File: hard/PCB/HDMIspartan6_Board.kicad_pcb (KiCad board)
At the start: 4 copper layers, 60 x 85.1 mm, 167 parts, among them IC1 W9812G6KH, J1 HDMI_A, P1 CONN_01X03, P2 CONN_01X02, P3 CONN_02X02, P4 CONN_02X02, P5 CONN_01X03, P6 CONN_01X03, P7 B6B-PH-K-S(LF)(SN), SW1 B3SL-1002P, U1 PAM8302AASCR, U2 TPS63070, X1 ASV-32.000MHZ-E-T

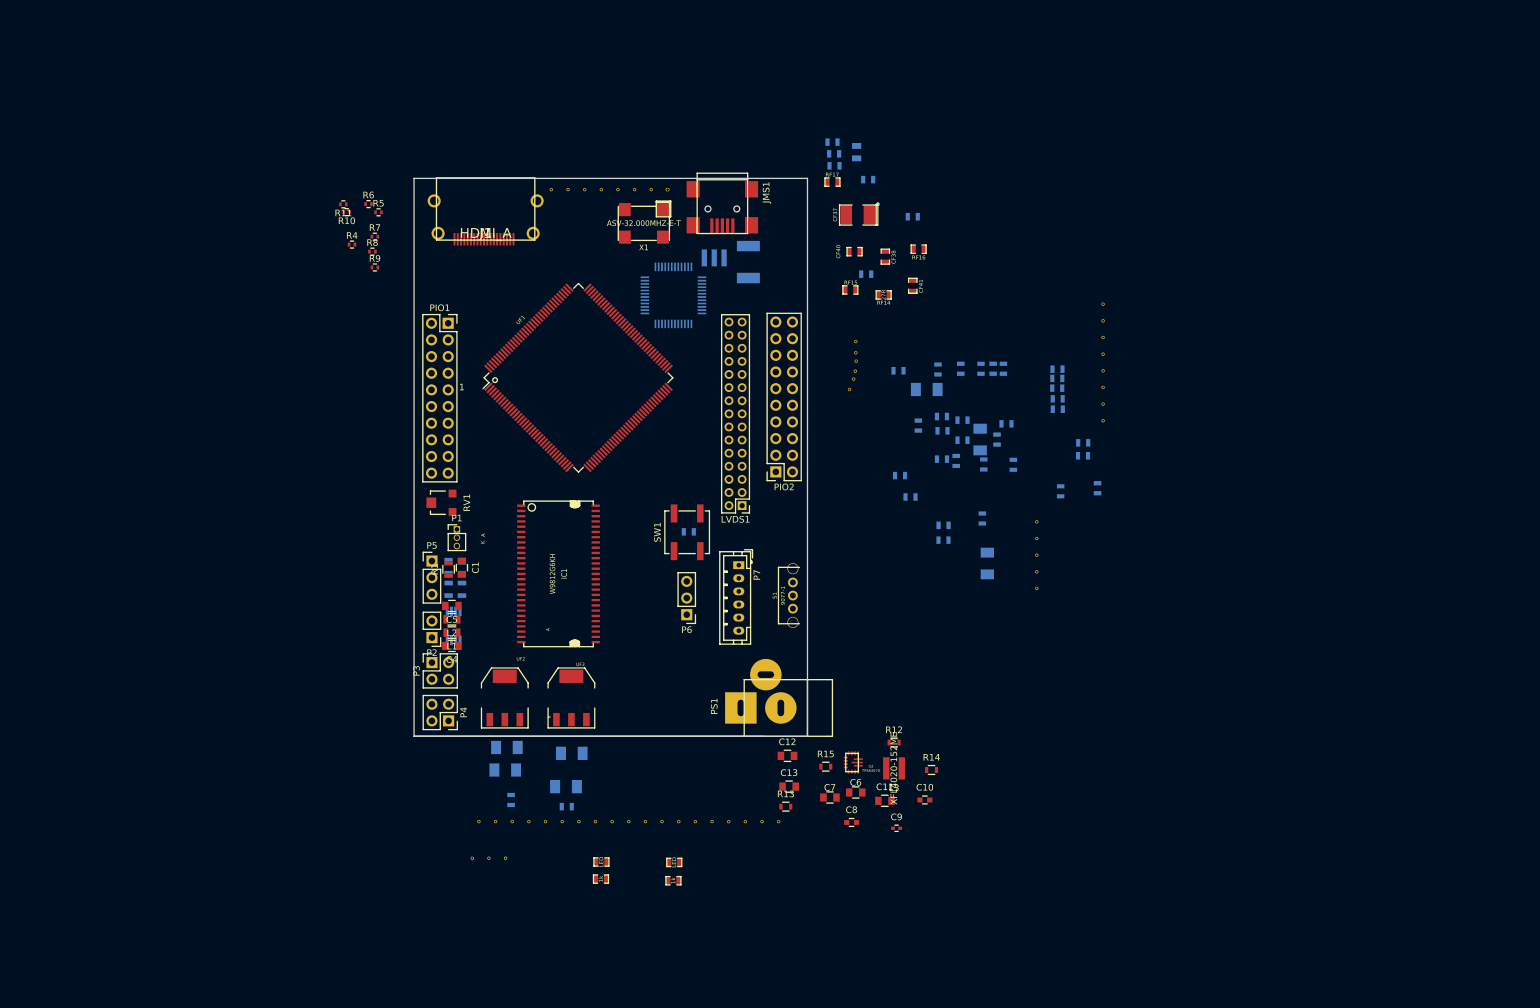
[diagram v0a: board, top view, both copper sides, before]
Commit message: Update supply power
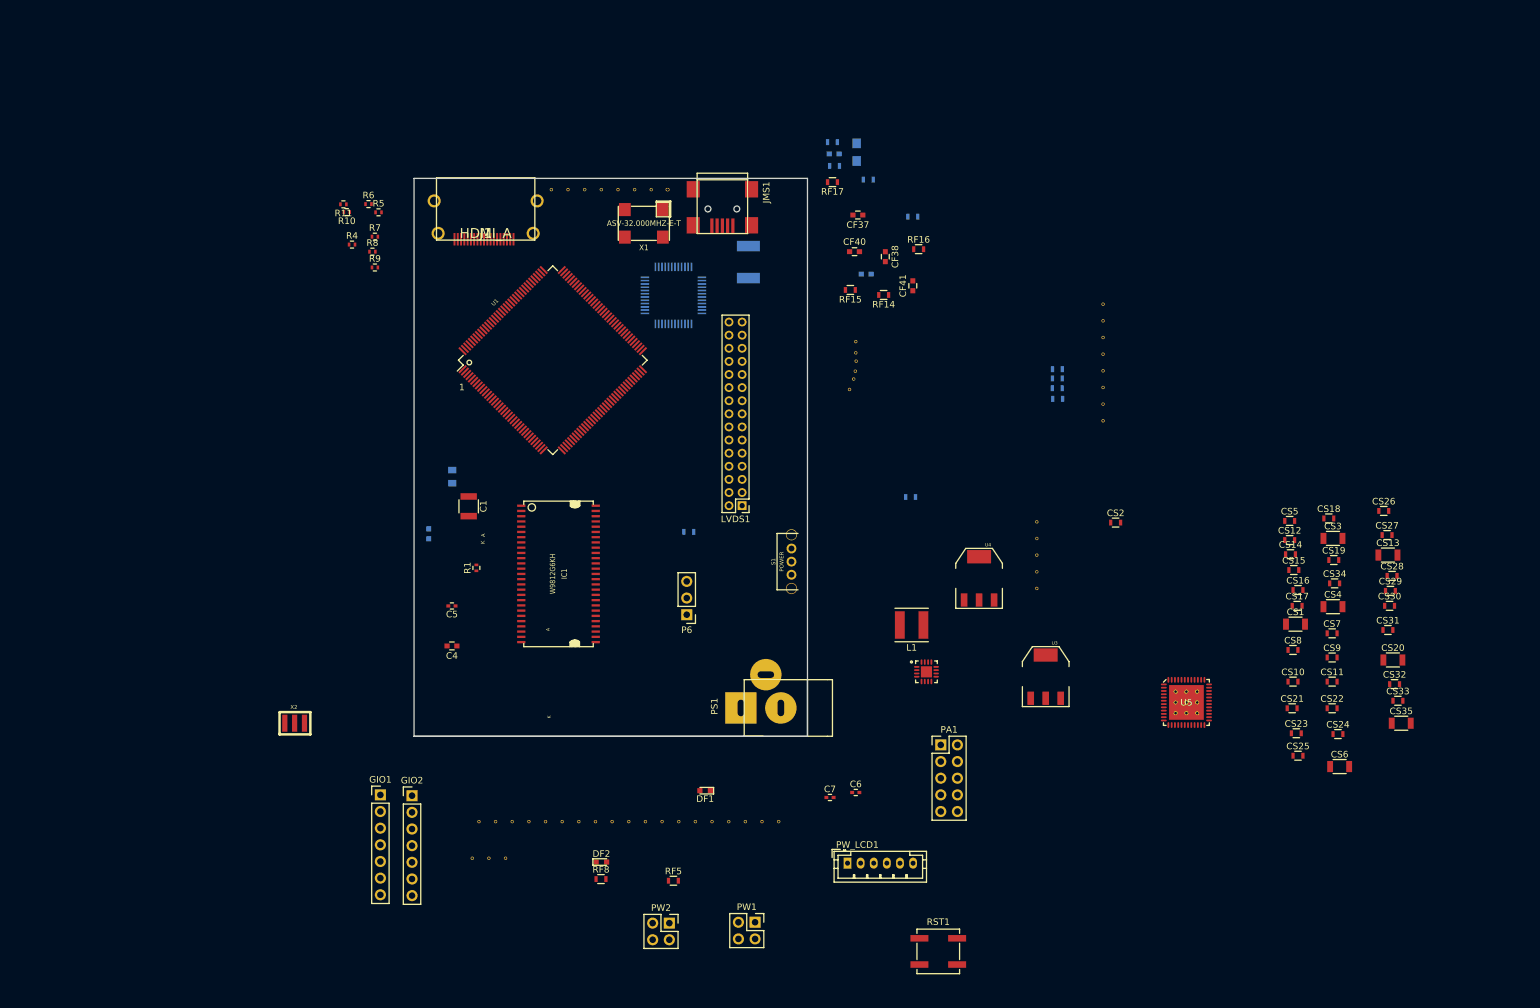
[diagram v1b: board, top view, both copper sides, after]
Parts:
- removed C10, C8: 10u, Capacitors_SMD:C_0603
- removed C11, C12, C13: 22u, Capacitors_SMD:C_0805
- removed C9: 100n, Capacitors_SMD:C_0402
- removed CF1, CF10, CF12, CF14, CF15, CF16, CF17, CF18, CF19, CF2, CF20, CF21, CF22, CF23, CF24, CF25, CF3, CF4, CF5, CF6, CF7, CF8, CF9: 0.1uF, opendous:SM0603
- removed CF11, CF26, CF27: 1uF, opendous:SM0603
- removed CF13, CF28, CF29: 4.7uF, opendous:SM1206_Opendous
- removed CF30, CF32, CF33, CF35: 33uF, opendous:SM1206_Opendous
- removed CF31, CF34: 100n, opendous:SM0603
- removed L2: Ferrite_Bead, Resistors_SMD:R_0805
- removed L3: XFL4020-152ME, resonator:XFL4020
- removed P1: CONN_01X03, Socket_Strips:Socket_Strip_Straight_1x03_Pitch1.27mm
- removed P2: CONN_01X02, Socket_Strips:Socket_Strip_Straight_1x02_Pitch2.54mm
- removed P3, P4: CONN_02X02, Socket_Strips:Socket_Strip_Straight_2x02_Pitch2.54mm
- removed P5: CONN_01X03, Socket_Strips:Socket_Strip_Straight_1x03_Pitch2.54mm
- removed P7: B6B-PH-K-S(LF)(SN), Connectors_JST:JST_PH_B6B-PH-K_06x2.00mm_Straight
- removed PIO1, PIO2: CONN_02X10, Socket_Strips:Socket_Strip_Straight_2x10_Pitch2.54mm
- removed R12: 10k, Resistors_SMD:R_0603
- removed R13: 680k, Resistors_SMD:R_0603
- removed R14: 130k, Resistors_SMD:R_0603
- removed R15: 100k, Resistors_SMD:R_0603
- removed R2, R3: 100, Resistors_SMD:R_0805
- removed RV1: 10K POT_TRIM, Potentiometers:Potentiometer_Trimmer-EVM3E
- removed SW1: B3SL-1002P, Buttons_Switches_SMD:SW_SPST_B3SL-1002P
- removed UF1: XC6SLX9-2TQG144C, Housings_QFP:LQFP-144_20x20mm_Pitch0.5mm
- removed UF2: ZLDO1117G33TA, SMD_Packages:SOT-223
- removed UF3: ZLDO1117G12TA, SMD_Packages:SOT-223
- removed XF2: 6MHz, resonator:CSTCR6M00G53Z
- added CS1: 33uF, Resistors_SMD:R_1206, F.Cu at (192.7, 100.0)
- added CS10: 0.1uF, Resistors_SMD:R_0603, F.Cu at (192.3, 108.7)
- added CS11: 0.1uF, Resistors_SMD:R_0603, F.Cu at (198.2, 108.7)
- added CS12: 1uF, Resistors_SMD:R_0603, F.Cu at (191.8, 87.1)
- added CS13: 4.7uF, Resistors_SMD:R_1206, F.Cu at (206.8, 89.4)
- added CS14: 1uF, Resistors_SMD:R_0603, F.Cu at (191.9, 89.3)
- added CS15: 1uF, Resistors_SMD:R_0603, F.Cu at (192.4, 91.7)
- added CS16: 1uF, Resistors_SMD:R_0603, F.Cu at (193.0, 94.7)
- added CS17: 1uF, Resistors_SMD:R_0603, F.Cu at (192.9, 97.2)
- added CS18: 1uF, Resistors_SMD:R_0603, F.Cu at (197.7, 83.8)
- added CS19: 1uF, Resistors_SMD:R_0603, F.Cu at (198.5, 90.2)
- added CS2: 100n, Resistors_SMD:R_0603, F.Cu at (165.2, 84.5)
- added CS20: 4.7uF, Resistors_SMD:R_1206, F.Cu at (207.5, 105.4)
- added CS21: 0.1uF, Resistors_SMD:R_0603, F.Cu at (192.2, 112.8)
- added CS22: 0.1uF, Resistors_SMD:R_0603, F.Cu at (198.2, 112.8)
- added CS23: 0.1uF, Resistors_SMD:R_0603, F.Cu at (192.8, 116.6)
- added CS24: 0.1uF, Resistors_SMD:R_0603, F.Cu at (199.1, 116.7)
- added CS25: 0.1uF, Resistors_SMD:R_0603, F.Cu at (193.0, 120.0)
- added CS26: 0.1uF, Resistors_SMD:R_0603, F.Cu at (206.1, 82.7)
- added CS27: 0.1uF, Resistors_SMD:R_0603, F.Cu at (206.6, 86.4)
- added CS28: 0.1uF, Resistors_SMD:R_0603, F.Cu at (207.4, 92.6)
- added CS29: 0.1uF, Resistors_SMD:R_0603, F.Cu at (207.1, 94.9)
- added CS3: 33uF, Resistors_SMD:R_1206, F.Cu at (198.4, 86.9)
- added CS30: 0.1uF, Resistors_SMD:R_0603, F.Cu at (207.0, 97.2)
- added CS31: 0.1uF, Resistors_SMD:R_0603, F.Cu at (206.8, 100.8)
- added CS32: 0.1uF, Resistors_SMD:R_0603, F.Cu at (207.8, 109.1)
- added CS33: 0.1uF, Resistors_SMD:R_0603, F.Cu at (208.3, 111.6)
- added CS34: 1uF, Resistors_SMD:R_0603, F.Cu at (198.6, 93.7)
- added CS35: 4.7uF, Resistors_SMD:R_1206, F.Cu at (208.8, 115.1)
- added CS4: 33uF, Resistors_SMD:R_1206, F.Cu at (198.4, 97.3)
- added CS5: 100n, Resistors_SMD:R_0603, F.Cu at (191.8, 84.2)
- added CS6: 33uF, Resistors_SMD:R_1206, F.Cu at (199.4, 121.7)
- added CS7: 0.1uF, Resistors_SMD:R_0603, F.Cu at (198.2, 101.3)
- added CS8: 0.1uF, Resistors_SMD:R_0603, F.Cu at (192.3, 103.9)
- added CS9: 0.1uF, Resistors_SMD:R_0603, F.Cu at (198.2, 105.0)
- added GIO1: CONN_01X07, Pin_Headers:Pin_Header_Straight_1x07_Pitch2.54mm, F.Cu at (53.1, 126.0)
- added GIO2: CONN_01X07, Pin_Headers:Pin_Header_Straight_1x07_Pitch2.54mm, F.Cu at (57.9, 126.1)
- added PA1: CONN_02X05, Pin_Headers:Pin_Header_Straight_2x05_Pitch2.54mm, F.Cu at (138.6, 118.4)
- added PW1: CONN_02X02, Socket_Strips:Socket_Strip_Straight_2x02_Pitch2.54mm, F.Cu at (110.2, 145.4)
- added PW2: CONN_02X02, Socket_Strips:Socket_Strip_Straight_2x02_Pitch2.54mm, F.Cu at (97.2, 145.5)
- added PW_LCD1: B6B-PH-K-S(LF)(SN), Connectors_JST:JST_PH_B6B-PH-K_06x2.00mm_Straight, F.Cu at (124.3, 136.4)
- added RST1: B3SL-1002P, Buttons_Switches_SMD:SW_SPST_B3SL-1002P, F.Cu at (138.2, 149.9)
- added U3: ZLDO1117G33TA, Project:SOT-223, F.Cu at (154.6, 108.0)
- added U4: ZLDO1117G12TA, Project:SOT-223, F.Cu at (144.4, 93.0)
- added U5: MAX5864, Project:GSG-QFN48-7, F.Cu at (176.0, 111.9)
- added X2: CSTCR6M00G53Z-R0, Project:CSTCR6M00G53Z, F.Cu at (40.0, 115.1)
- C1: footprint Capacitors_SMD:C_0805 -> Capacitors_SMD:C_1210
- C2: value 1uF -> 100nF; footprint Capacitors_SMD:C_0805 -> Capacitors_SMD:C_0603
- C3: value 1uF -> 22uF
- C4: value 220pF -> 3.3nF; footprint Capacitors_SMD:C_0805 -> Capacitors_SMD:C_0603
- C5: value 220pF -> 330nF; footprint Capacitors_SMD:C_0805 -> Capacitors_SMD:C_0402
- C6, C7: value 10u -> 330nF; footprint Capacitors_SMD:C_0805 -> Capacitors_SMD:C_0402
- CF36, CF38, CF39, CF40, CF41: footprint opendous:SM0603_Opendous -> Capacitors_SMD:C_0603
- CF37: footprint opendous:SM1210_Opendous -> Capacitors_SMD:C_0603
- DF1, DF2: footprint opendous:SM0603 -> LEDs:LED_0603
- FT1: footprint Housings_QFP:LQFP-48_7x7mm_Pitch0.5mm -> Project:LQFP-48_7x7mm_Pitch0.5mm
- IC1: footprint opendous:TSOPII54_SDRAM_MT48 -> Project:TSOPII54_SDRAM_MT48
- J1: footprint HDMI:FCI_10029449-11[13]RLF -> Project:HDMI_FCI_10029449-11[13]RLF
- JMS1: footprint Connect:USB_Mini-B -> Project:USB_Mini-B
- L1: value Ferrite_Bead -> VLS5045EX-2R2N; footprint Resistors_SMD:R_0805 -> Inductors:Inductor_Taiyo-Yuden_NR-50xx
- LF11: footprint opendous:SM0805 -> Resistors_SMD:R_0805_HandSoldering
- PS1: footprint Connect:JACK_ALIM -> Project:JACK_ALIM
- R1: value 10k -> 0R; footprint Resistors_SMD:R_0805 -> Resistors_SMD:R_0402
- RF1, RF3, RF4, RF8: footprint opendous:SM0603 -> Resistors_SMD:R_0603
- RF14, RF15, RF16, RF17, RF18, RF19, RF20, RF21: footprint opendous:SM0603_Opendous -> Resistors_SMD:R_0603
- RF2: value 4.7k -> 68; footprint opendous:SM0603 -> Resistors_SMD:R_0603
- RF5: value 1k -> 68; footprint opendous:SM0603 -> Resistors_SMD:R_0603
- RF6: value 68 -> 4.7k; footprint opendous:SM0603 -> Resistors_SMD:R_0603
- RF7: value 68 -> 1k; footprint opendous:SM0603 -> Resistors_SMD:R_0603
- S1: value 9077-1 -> POWER; footprint resonator:CKCOMP-OS102011MA1QN1 -> Project:CKCOMP-OS102011MA1QN1
- U1: value PAM8302AASCR -> XC6SLX9-2TQG144C; footprint Housings_SSOP:MSOP-8_3x3mm_Pitch0.65mm -> Project:LQFP-144_20x20mm_Pitch0.5mm; moved to F.Cu
- U2: value TPS63070 -> TPS62133RGTR; footprint resonator:TPS63071 -> Project:QFN16
- X1: footprint opendous:OSCILLATOR_7x5mm -> Project:OSCILLATOR_7x5mm
- moved L1 70.1 mm to (134.1, 100.1)
- moved U1 43.3 mm to (79.4, 59.7), turned to 45 degrees
- moved U2 17.8 mm to (136.4, 107.2)
- moved C3 14.0 mm to (64.0, 77.5)
- moved DF1 11.9 mm to (102.6, 125.4)
- moved C1 9.41 mm to (66.6, 82.0)
- moved C2 5.99 mm to (60.5, 86.2)
- moved S1 5.18 mm to (115.8, 90.4)
- moved R1 4.24 mm to (67.7, 91.4)
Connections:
- C1 pad 1: +5V -> +9V
- C2 pad 1: Net-(C2-Pad1) -> +9V
- C2 pad 2: Net-(C2-Pad2) -> GND
- C3 pad 1: Net-(C3-Pad1) -> VDD5V
- C3 pad 2: /Audio/AIN- -> GND
- C4 pad 1: GND -> Net-(C4-Pad1)
- C4 pad 2: Net-(C4-Pad2) -> GND
- C5 pad 1: GND -> /Anlg_Front_End/COM
- C5 pad 2: Net-(C5-Pad2) -> GND
- C6 pad 1: /Power/+9V0 -> /Anlg_Front_End/REFN
- C7 pad 1: /Power/+9V0 -> /Anlg_Front_End/REFP
- DF1 pad 1: Net-(DF1-Pad1) -> (no net)
- DF2 pad 1: Net-(DF2-Pad1) -> (no net)
- FT1 pad 1: Net-(FT1-Pad1) -> (no net)
- FT1 pad 11: Net-(FT1-Pad11) -> (no net)
- FT1 pad 12: Net-(FT1-Pad12) -> (no net)
- FT1 pad 13: Net-(FT1-Pad13) -> (no net)
- FT1 pad 15: Net-(FT1-Pad15) -> (no net)
- FT1 pad 16: Net-(FT1-Pad16) -> (no net)
- FT1 pad 17: Net-(FT1-Pad17) -> (no net)
- FT1 pad 19: Net-(FT1-Pad19) -> (no net)
- FT1 pad 20: Net-(FT1-Pad20) -> (no net)
- FT1 pad 27: Net-(FT1-Pad27) -> (no net)
- FT1 pad 28: Net-(FT1-Pad28) -> (no net)
- FT1 pad 29: Net-(FT1-Pad29) -> (no net)
- FT1 pad 30: Net-(FT1-Pad30) -> (no net)
- FT1 pad 32: Net-(FT1-Pad32) -> (no net)
- FT1 pad 33: Net-(FT1-Pad33) -> (no net)
- FT1 pad 35: Net-(FT1-Pad35) -> (no net)
- FT1 pad 36: Net-(FT1-Pad36) -> (no net)
- FT1 pad 37: Net-(FT1-Pad37) -> (no net)
- FT1 pad 38: Net-(FT1-Pad38) -> (no net)
- FT1 pad 41: Net-(FT1-Pad41) -> (no net)
- FT1 pad 48: Net-(FT1-Pad48) -> (no net)
- J1 pad 13: Net-(J1-Pad13) -> (no net)
- J1 pad 14: Net-(J1-Pad14) -> (no net)
- J1 pad 15: Net-(J1-Pad15) -> (no net)
- J1 pad 16: Net-(J1-Pad16) -> (no net)
- J1 pad 17: Net-(J1-Pad17) -> (no net)
- J1 pad 18: Net-(J1-Pad18) -> (no net)
- J1 pad 19: Net-(J1-Pad19) -> (no net)
- JMS1 pad 4: Net-(JMS1-Pad4) -> (no net)
- L1 pad 1: Net-(L1-Pad1) -> VDD5V
- L1 pad 2: Net-(C4-Pad2) -> Net-(L1-Pad2)
- LVDS1 pad 19: Net-(LVDS1-Pad19) -> (no net)
- LVDS1 pad 20: Net-(LVDS1-Pad20) -> (no net)
- LVDS1 pad 21: Net-(LVDS1-Pad21) -> (no net)
- LVDS1 pad 22: Net-(LVDS1-Pad22) -> (no net)
- LVDS1 pad 23: Net-(LVDS1-Pad23) -> (no net)
- LVDS1 pad 24: Net-(LVDS1-Pad24) -> (no net)
- LVDS1 pad 25: Net-(LVDS1-Pad25) -> (no net)
- LVDS1 pad 26: Net-(LVDS1-Pad26) -> (no net)
- LVDS1 pad 27: Net-(LVDS1-Pad27) -> (no net)
- LVDS1 pad 28: Net-(LVDS1-Pad28) -> (no net)
- LVDS1 pad 29: Net-(LVDS1-Pad29) -> (no net)
- LVDS1 pad 30: Net-(LVDS1-Pad30) -> (no net)
- PS1 pad 1: +9V -> VCC
- PS1 pad 3: Net-(PS1-Pad3) -> (no net)
- R1 pad 1: /spartan6/F_~SD -> /Power/PG
- R1 pad 2: +5V -> Net-(R1-Pad2)
- RF2 pad 1: Net-(RF2-Pad1) -> /spartan6/F_TDI
- RF2 pad 2: +3V3 -> Net-(RF2-Pad2)
- RF3 pad 1: /spartan6/F_TDI -> /spartan6/F_TDO
- RF5 pad 1: GND -> /spartan6/F_TMS
- RF5 pad 2: Net-(DF1-Pad2) -> Net-(RF5-Pad2)
- RF6 pad 1: /spartan6/F_TMS -> +3V3
- RF7 pad 1: /spartan6/F_TDO -> GND
- RF7 pad 2: Net-(RF7-Pad2) -> Net-(DF2-Pad2)
- RF8 pad 2: Net-(DF2-Pad2) -> Net-(DF1-Pad2)
- S1 pad 1: +9V -> VCC
- S1 pad 2: /Power/+9V0 -> +9V
- S1 pad 3: Net-(S1-Pad3) -> (no net)
- U1 pad 1: /spartan6/F_~SD -> /spartan6/~CS
- U1 pad 2: Net-(U1-Pad2) -> /spartan6/~RAS
- U1 pad 3: Net-(R2-Pad1) -> GND
- U1 pad 4: Net-(R3-Pad1) -> +3V3
- U1 pad 5: Net-(L2-Pad1) -> /spartan6/~CAS
- U1 pad 6: +5V -> /spartan6/~WE
- U1 pad 7: GND -> /spartan6/DQML
- U1 pad 8: Net-(L1-Pad1) -> /spartan6/DQ7
- U2 pad 1: Net-(R12-Pad2) -> Net-(L1-Pad2)
- U2 pad 10: GND -> +9V
- U2 pad 11: Net-(L3-Pad1) -> +9V
- U2 pad 12: /Power/+9V0 -> +9V
- U2 pad 13: /Power/+9V0 -> +9V
- U2 pad 14: Net-(R12-Pad2) -> VDD5V
- U2 pad 2: Net-(R15-Pad2) -> Net-(L1-Pad2)
- U2 pad 3: Net-(C9-Pad1) -> Net-(L1-Pad2)
- U2 pad 4: GND -> /Power/PG
- U2 pad 5: Net-(R13-Pad2) -> GND
- U2 pad 7: VDD5V -> Net-(R1-Pad2)
- U2 pad 8: VDD5V -> GND
- U2 pad 9: Net-(L3-Pad2) -> Net-(C4-Pad1)
- X1 pad 3: /spartan6/FPGA_CLK -> /spartan6/FPGA_CK

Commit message: Corrección esquematico
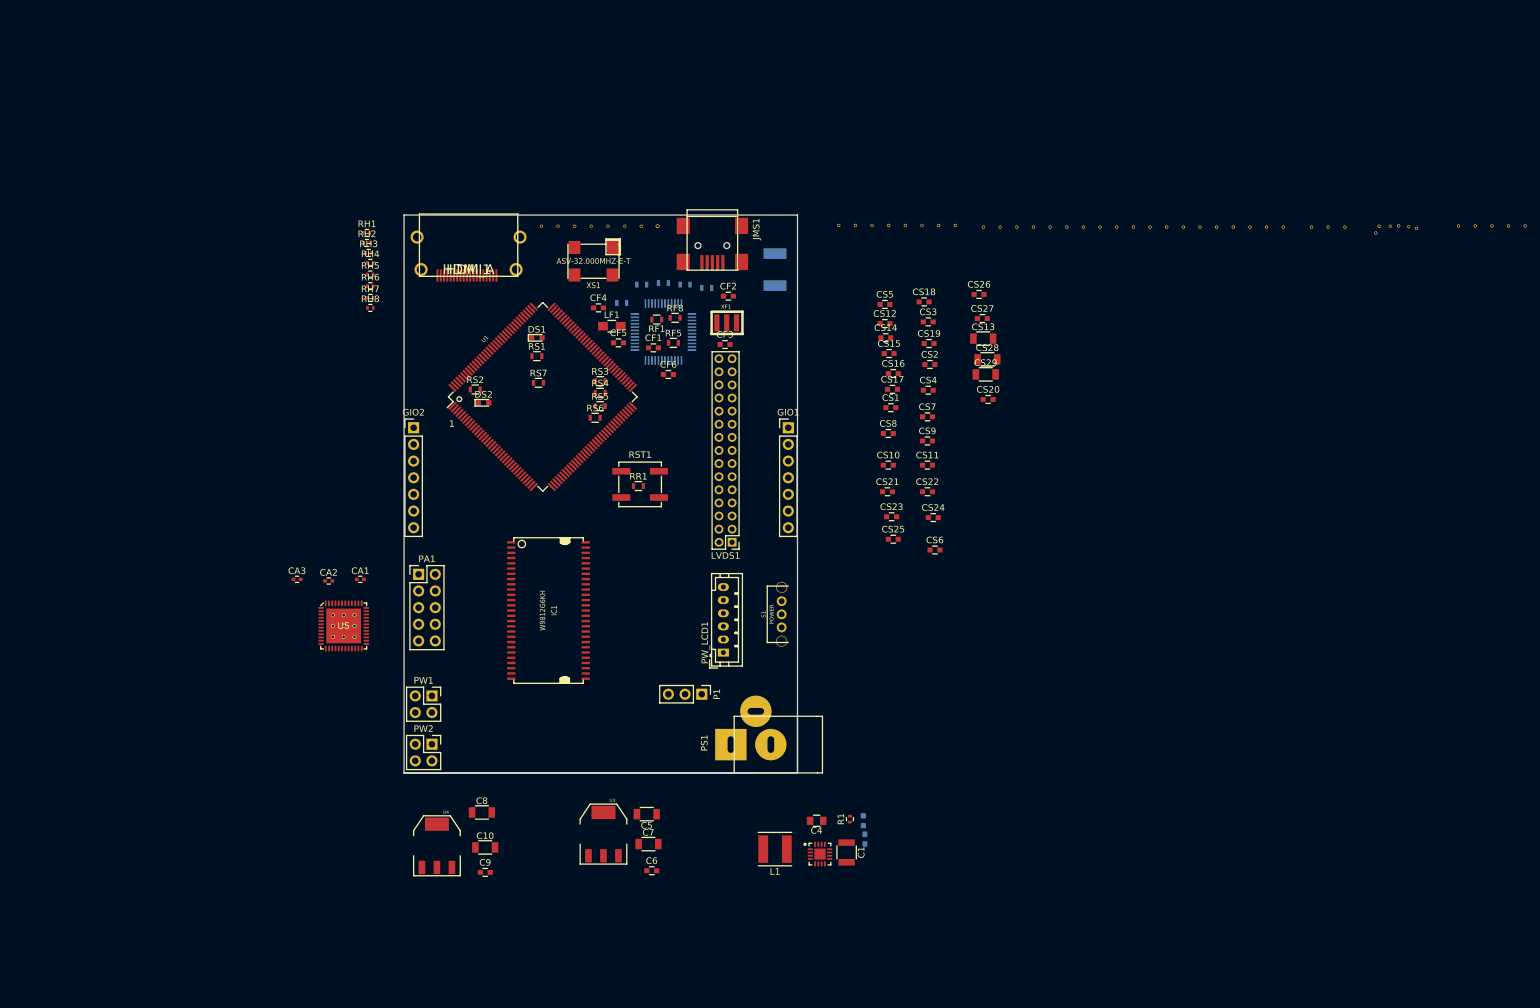
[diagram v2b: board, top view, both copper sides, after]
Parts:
- removed CF36: 10nF, Capacitors_SMD:C_0603
- removed CF37: 10uF, Capacitors_SMD:C_0603
- removed CF38: 100nF, Capacitors_SMD:C_0603
- removed CF39: 33nF, Capacitors_SMD:C_0603
- removed CF40, CF41: 47pF, Capacitors_SMD:C_0603
- removed CS30, CS31, CS32, CS33: 0.1uF, Resistors_SMD:R_0603
- removed CS34: 1uF, Resistors_SMD:R_0603
- removed CS35: 4.7uF, Resistors_SMD:R_1206
- removed DF1, DF2: LED, LEDs:LED_0603
- removed J1: HDMI_A, Project:HDMI_FCI_10029449-11[13]RLF
- removed LF11: HZ0805D152R-10, Resistors_SMD:R_0805_HandSoldering
- removed P6: CONN_01X03, Socket_Strips:Socket_Strip_Straight_1x03_Pitch2.54mm
- removed R10, R11, R4, R5, R6, R7, R8, R9: 51, Resistors_SMD:R_0402
- removed RF14, RF15: 27R, Resistors_SMD:R_0603
- removed RF16: 10K, Resistors_SMD:R_0603
- removed RF17: 1K5, Resistors_SMD:R_0603
- removed RF18: 470R, Resistors_SMD:R_0603
- removed RF19, RF20: 10k, Resistors_SMD:R_0603
- removed RF21: 15K, Resistors_SMD:R_0603
- removed X1: ASV-32.000MHZ-E-T, Project:OSCILLATOR_7x5mm
- removed X2: CSTCR6M00G53Z-R0, Project:CSTCR6M00G53Z
- added C10: 33uF, Capacitors_SMD:C_1206, F.Cu at (69.1, 134.0)
- added C8: 33uF, Capacitors_SMD:C_1206, F.Cu at (68.6, 128.7)
- added C9: 100n, Capacitors_SMD:C_0603, F.Cu at (69.1, 137.8)
- added CA1: 330nF, Capacitors_SMD:C_0402, F.Cu at (50.0, 93.1)
- added CA2: 330nF, Capacitors_SMD:C_0402, F.Cu at (45.2, 93.4)
- added CA3: 330nF, Capacitors_SMD:C_0402, F.Cu at (40.4, 93.1)
- added CF1: 47pF, Capacitors_SMD:C_0603, F.Cu at (94.7, 57.8)
- added CF2: 47pF, Capacitors_SMD:C_0603, F.Cu at (106.2, 49.9)
- added CF3: 10nF, Capacitors_SMD:C_0603, F.Cu at (105.7, 57.3)
- added CF4: 10uF, Capacitors_SMD:C_0603, F.Cu at (86.3, 51.7)
- added CF5: 33nF, Capacitors_SMD:C_0603, F.Cu at (89.4, 57.0)
- added CF6: 100nF, Capacitors_SMD:C_0603, F.Cu at (97.0, 61.9)
- added DS1: LED, LEDs:LED_0603, F.Cu at (77.0, 56.3)
- added DS2: LED, LEDs:LED_0603, F.Cu at (68.8, 66.2)
- added HDMI1: HDMI_A, Project:HDMI_FCI_10029449-11[13]RLF, F.Cu at (66.5, 45.9)
- added LF1: HZ0805D152R-10, Resistors_SMD:R_0805_HandSoldering, F.Cu at (88.4, 54.5)
- added P1: CONN_01X03, Socket_Strips:Socket_Strip_Straight_1x03_Pitch2.54mm, F.Cu at (102.1, 110.6)
- added RH1: 51, Resistors_SMD:R_0402, F.Cu at (51.0, 40.3)
- added RH2: 51, Resistors_SMD:R_0402, F.Cu at (51.0, 41.8)
- added RH3: 51, Resistors_SMD:R_0402, F.Cu at (51.3, 43.3)
- added RH4: 51, Resistors_SMD:R_0402, F.Cu at (51.6, 44.9)
- added RH5: 51, Resistors_SMD:R_0402, F.Cu at (51.6, 46.6)
- added RH6: 51, Resistors_SMD:R_0402, F.Cu at (51.6, 48.4)
- added RH7: 51, Resistors_SMD:R_0402, F.Cu at (51.6, 50.2)
- added RH8: 51, Resistors_SMD:R_0402, F.Cu at (51.6, 51.7)
- added RR1: 47k, Resistors_SMD:R_0603, F.Cu at (92.4, 78.9)
- added RS1: 1k, Resistors_SMD:R_0603, F.Cu at (77.0, 59.1)
- added RS2: 1k, Resistors_SMD:R_0603, F.Cu at (67.6, 64.2)
- added RS3: 68, Resistors_SMD:R_0603, F.Cu at (86.6, 62.9)
- added RS4: 68, Resistors_SMD:R_0603, F.Cu at (86.6, 64.7)
- added RS5: 68, Resistors_SMD:R_0603, F.Cu at (86.6, 66.7)
- added RS6: 68, Resistors_SMD:R_0603, F.Cu at (85.8, 68.5)
- added RS7: 4.7k, Resistors_SMD:R_0603, F.Cu at (77.2, 63.1)
- added XF1: CSTCR6M00G53Z-R0, Project:CSTCR6M00G53Z, F.Cu at (105.9, 54.0)
- added XS1: ASV-32.000MHZ-E-T, Project:OSCILLATOR_7x5mm, F.Cu at (85.6, 44.6)
- C3: value 22uF -> 3.3nF; footprint Capacitors_SMD:C_0805 -> Capacitors_SMD:C_0603
- C4: value 3.3nF -> 22uF; footprint Capacitors_SMD:C_0603 -> Capacitors_SMD:C_0805
- C5, C7: value 330nF -> 33uF; footprint Capacitors_SMD:C_0402 -> Capacitors_SMD:C_1206
- C6: value 330nF -> 100n; footprint Capacitors_SMD:C_0402 -> Capacitors_SMD:C_0603
- CS1, CS3, CS4, CS6: value 33uF -> 0.1uF; footprint Resistors_SMD:R_1206 -> Capacitors_SMD:C_0603
- CS10, CS21, CS22, CS23, CS24, CS25, CS7, CS8, CS9: footprint Resistors_SMD:R_0603 -> Capacitors_SMD:C_0603
- CS11, CS26, CS27: value 0.1uF -> 1uF; footprint Resistors_SMD:R_0603 -> Capacitors_SMD:C_0603
- CS12, CS14, CS15, CS16, CS17, CS18, CS19: value 1uF -> 0.1uF; footprint Resistors_SMD:R_0603 -> Capacitors_SMD:C_0603
- CS13: footprint Resistors_SMD:R_1206 -> Capacitors_SMD:C_1206
- CS2, CS5: value 100n -> 0.1uF; footprint Resistors_SMD:R_0603 -> Capacitors_SMD:C_0603
- CS20: value 4.7uF -> 0.1uF; footprint Resistors_SMD:R_1206 -> Capacitors_SMD:C_0603
- CS28, CS29: value 0.1uF -> 4.7uF; footprint Resistors_SMD:R_0603 -> Capacitors_SMD:C_1206
- RF1: value 47k -> 27R; moved to F.Cu
- RF2: value 68 -> 27R
- RF3: value 68 -> 1K5
- RF4: value 68 -> 10K
- RF5: value 68 -> 470R
- RF6: value 4.7k -> 10k
- RF7: value 1k -> 10k
- RF8: value 1k -> 15K
- TH1, TH10, TH11, TH12, TH13, TH14, TH15, TH16, TH17, TH18, TH19, TH2, TH20, TH21, TH22, TH23, TH24, TH25, TH26, TH27, TH28, TH29, TH3, TH30, TH31, TH32, TH33, TH34, TH35, TH36, TH37, TH38, TH39, TH4, TH40, TH41, TH42, TH43, TH44, TH45, TH46, TH47, TH48, TH49, TH5, TH50, TH6, TH7, TH8, TH9: footprint opendous:1Pin_12mil_VIA -> Project:1Pin_12mil_VIA
- moved TH1 160.2 mm to (195.1, 39.4)
- moved TH12 160.2 mm to (197.7, 39.4)
- moved TH15 160.2 mm to (200.2, 39.4)
- moved U5 129.1 mm to (47.5, 100.2)
- moved TH10 118.9 mm to (147.6, 39.4)
- moved TH11 118.9 mm to (185.7, 39.4)
- moved TH16 118.9 mm to (175.6, 39.4)
- moved TH18 118.9 mm to (157.8, 39.4)
- moved TH19 118.9 mm to (155.2, 39.4)
- moved TH2 118.9 mm to (162.9, 39.4)
- moved TH20 118.9 mm to (165.4, 39.4)
- moved TH34 118.9 mm to (190.8, 39.4)
- moved TH4 118.9 mm to (173.0, 39.4)
- moved TH6 118.9 mm to (145.1, 39.4)
- moved TH8 118.9 mm to (180.6, 39.4)
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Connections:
- net /Anlg_Front_End/IA+ renamed /ADC_DAC/IA+
- net /Anlg_Front_End/IA- renamed /ADC_DAC/IA-
- net /Anlg_Front_End/ID+ renamed /ADC_DAC/ID+
- net /Anlg_Front_End/ID- renamed /ADC_DAC/ID-
- net /Anlg_Front_End/QA+ renamed /ADC_DAC/QA+
- net /Anlg_Front_End/QA- renamed /ADC_DAC/QA-
- net /Anlg_Front_End/QD+ renamed /ADC_DAC/QD+
- net /Anlg_Front_End/QD- renamed /ADC_DAC/QD-
- C3 pad 1: VDD5V -> Net-(C3-Pad1)
- C4 pad 1: Net-(C4-Pad1) -> VDD5V
- C5 pad 1: /Anlg_Front_End/COM -> +5V
- C6 pad 1: /Anlg_Front_End/REFN -> +3V3
- C7 pad 1: /Anlg_Front_End/REFP -> +3V3
- CS1 pad 1: +5V -> +3V3
- CS14 pad 1: +1V2 -> +3V3
- CS15 pad 1: +1V2 -> +3V3
- CS16 pad 1: +1V2 -> +3V3
- CS18 pad 1: +1V2 -> +3V3
- CS20 pad 1: +1V2 -> +3V3
- CS21 pad 1: +3V3 -> +1V2
- CS23 pad 1: +3V3 -> +1V2
- CS25 pad 1: +3V3 -> +1V2
- CS27 pad 1: +3V3 -> +1V2
- CS29 pad 1: +3V3 -> +1V2
- CS5 pad 1: +1V2 -> +3V3
- CS6 pad 1: +1V2 -> +3V3
- FT1 pad 1: (no net) -> Net-(FT1-Pad1)
- FT1 pad 11: (no net) -> Net-(FT1-Pad11)
- FT1 pad 12: (no net) -> Net-(FT1-Pad12)
- FT1 pad 13: (no net) -> Net-(FT1-Pad13)
- FT1 pad 15: (no net) -> Net-(FT1-Pad15)
- FT1 pad 16: (no net) -> Net-(FT1-Pad16)
- FT1 pad 17: (no net) -> Net-(FT1-Pad17)
- FT1 pad 19: (no net) -> Net-(FT1-Pad19)
- FT1 pad 20: (no net) -> Net-(FT1-Pad20)
- FT1 pad 27: (no net) -> Net-(FT1-Pad27)
- FT1 pad 28: (no net) -> Net-(FT1-Pad28)
- FT1 pad 29: (no net) -> Net-(FT1-Pad29)
- FT1 pad 30: (no net) -> Net-(FT1-Pad30)
- FT1 pad 32: (no net) -> Net-(FT1-Pad32)
- FT1 pad 33: (no net) -> Net-(FT1-Pad33)
- FT1 pad 35: (no net) -> Net-(FT1-Pad35)
- FT1 pad 36: (no net) -> Net-(FT1-Pad36)
- FT1 pad 37: (no net) -> Net-(FT1-Pad37)
- FT1 pad 38: (no net) -> Net-(FT1-Pad38)
- FT1 pad 41: (no net) -> Net-(FT1-Pad41)
- FT1 pad 46: Net-(CF38-Pad1) -> Net-(CF6-Pad1)
- FT1 pad 48: (no net) -> Net-(FT1-Pad48)
- GIO1 pad 1: (no net) -> Net-(GIO1-Pad1)
- GIO1 pad 2: (no net) -> Net-(GIO1-Pad2)
- GIO1 pad 3: (no net) -> Net-(GIO1-Pad3)
- GIO1 pad 4: (no net) -> Net-(GIO1-Pad4)
- GIO1 pad 5: (no net) -> Net-(GIO1-Pad5)
- GIO1 pad 6: (no net) -> Net-(GIO1-Pad6)
- GIO1 pad 7: (no net) -> Net-(GIO1-Pad7)
- GIO2 pad 1: (no net) -> Net-(GIO2-Pad1)
- GIO2 pad 2: (no net) -> Net-(GIO2-Pad2)
- GIO2 pad 3: (no net) -> Net-(GIO2-Pad3)
- GIO2 pad 4: (no net) -> Net-(GIO2-Pad4)
- GIO2 pad 5: (no net) -> Net-(GIO2-Pad5)
- GIO2 pad 6: (no net) -> Net-(GIO2-Pad6)
- GIO2 pad 7: (no net) -> Net-(GIO2-Pad7)
- JMS1 pad 4: (no net) -> Net-(JMS1-Pad4)
- LVDS1 pad 19: (no net) -> Net-(LVDS1-Pad19)
- LVDS1 pad 20: (no net) -> Net-(LVDS1-Pad20)
- LVDS1 pad 21: (no net) -> Net-(LVDS1-Pad21)
- LVDS1 pad 22: (no net) -> Net-(LVDS1-Pad22)
- LVDS1 pad 23: (no net) -> Net-(LVDS1-Pad23)
- LVDS1 pad 24: (no net) -> Net-(LVDS1-Pad24)
- LVDS1 pad 25: (no net) -> Net-(LVDS1-Pad25)
- LVDS1 pad 26: (no net) -> Net-(LVDS1-Pad26)
- LVDS1 pad 27: (no net) -> Net-(LVDS1-Pad27)
- LVDS1 pad 28: (no net) -> Net-(LVDS1-Pad28)
- LVDS1 pad 29: (no net) -> Net-(LVDS1-Pad29)
- LVDS1 pad 30: (no net) -> Net-(LVDS1-Pad30)
- PS1 pad 3: (no net) -> Net-(PS1-Pad3)
- PW_LCD1 pad 3: (no net) -> Net-(PW_LCD1-Pad3)
- RF1 pad 1: +3V3 -> Net-(JMS1-Pad2)
- RF1 pad 2: /spartan6/REBOOT -> Net-(FT1-Pad8)
- RF2 pad 1: /spartan6/F_TDI -> Net-(JMS1-Pad3)
- RF2 pad 2: Net-(RF2-Pad2) -> Net-(FT1-Pad7)
- RF3 pad 1: /spartan6/F_TDO -> Net-(FT1-Pad7)
- RF3 pad 2: Net-(RF3-Pad2) -> Net-(FT1-Pad5)
- RF4 pad 1: /spartan6/F_TCK -> /serial_interface/+5VA
- RF4 pad 2: Net-(RF4-Pad2) -> Net-(FT1-Pad2)
- RF5 pad 1: /spartan6/F_TMS -> Net-(CF6-Pad1)
- RF5 pad 2: Net-(RF5-Pad2) -> /serial_interface/+5VA
- RF6 pad 1: +3V3 -> Net-(FT1-Pad10)
- RF6 pad 2: Net-(RF6-Pad2) -> +3V3
- RF7 pad 1: GND -> Net-(FT1-Pad26)
- RF7 pad 2: Net-(DF2-Pad2) -> +3V3
- RF8 pad 1: GND -> +3V3
- RF8 pad 2: Net-(DF1-Pad2) -> /spartan6/F_RXD
- S1 pad 3: (no net) -> Net-(S1-Pad3)
- U1 pad 100: (no net) -> Net-(U1-Pad100)
- U1 pad 102: (no net) -> Net-(U1-Pad102)
- U1 pad 104: (no net) -> Net-(U1-Pad104)
- U1 pad 106: Net-(RF3-Pad2) -> Net-(RS5-Pad2)
- U1 pad 107: Net-(RF5-Pad2) -> Net-(RS6-Pad2)
- U1 pad 109: Net-(RF4-Pad2) -> Net-(RS3-Pad2)
- U1 pad 110: Net-(RF2-Pad2) -> Net-(RS4-Pad2)
- U1 pad 116: (no net) -> Net-(U1-Pad116)
- U1 pad 117: (no net) -> Net-(U1-Pad117)
- U1 pad 120: (no net) -> Net-(U1-Pad120)
- U1 pad 121: (no net) -> Net-(U1-Pad121)
- U1 pad 123: (no net) -> Net-(U1-Pad123)
- U1 pad 124: (no net) -> Net-(U1-Pad124)
- U1 pad 126: (no net) -> Net-(U1-Pad126)
- U1 pad 127: (no net) -> Net-(U1-Pad127)
- U1 pad 131: (no net) -> Net-(U1-Pad131)
- U1 pad 132: (no net) -> Net-(U1-Pad132)
- U1 pad 34: (no net) -> Net-(U1-Pad34)
- U1 pad 38: Net-(RF6-Pad2) -> Net-(RS7-Pad2)
- U1 pad 39: (no net) -> Net-(U1-Pad39)
- U1 pad 47: (no net) -> Net-(U1-Pad47)
- U1 pad 48: (no net) -> Net-(U1-Pad48)
- U1 pad 59: (no net) -> Net-(U1-Pad59)
- U1 pad 66: (no net) -> Net-(U1-Pad66)
- U1 pad 67: (no net) -> Net-(U1-Pad67)
- U1 pad 70: (no net) -> Net-(U1-Pad70)
- U1 pad 71: (no net) -> Net-(U1-Pad71)
- U1 pad 72: (no net) -> Net-(U1-Pad72)
- U1 pad 73: (no net) -> Net-(U1-Pad73)
- U1 pad 74: (no net) -> Net-(U1-Pad74)
- U1 pad 75: (no net) -> Net-(U1-Pad75)
- U1 pad 78: (no net) -> Net-(U1-Pad78)
- U1 pad 79: (no net) -> Net-(U1-Pad79)
- U1 pad 80: (no net) -> Net-(U1-Pad80)
- U1 pad 81: (no net) -> Net-(U1-Pad81)
- U1 pad 82: (no net) -> Net-(U1-Pad82)
- U1 pad 83: (no net) -> Net-(U1-Pad83)
- U1 pad 84: (no net) -> Net-(U1-Pad84)
- U1 pad 85: (no net) -> Net-(U1-Pad85)
- U1 pad 87: (no net) -> Net-(U1-Pad87)
- U1 pad 88: (no net) -> Net-(U1-Pad88)
- U1 pad 92: (no net) -> Net-(U1-Pad92)
- U1 pad 93: (no net) -> Net-(U1-Pad93)
- U1 pad 95: (no net) -> Net-(U1-Pad95)
- U1 pad 97: (no net) -> Net-(U1-Pad97)
- U1 pad 98: (no net) -> Net-(U1-Pad98)
- U1 pad 99: (no net) -> Net-(U1-Pad99)
- U2 pad 9: Net-(C4-Pad1) -> Net-(C3-Pad1)
- U5 pad 1: /Anlg_Front_End/REFP -> /ADC_DAC/REFP
- U5 pad 13: (no net) -> /ADC_DAC/DA0
- U5 pad 14: (no net) -> /ADC_DAC/DA1
- U5 pad 15: (no net) -> /ADC_DAC/DA2
- U5 pad 16: (no net) -> /ADC_DAC/DA3
- U5 pad 19: (no net) -> /ADC_DAC/DA4
- U5 pad 20: (no net) -> /ADC_DAC/DA5
- U5 pad 21: (no net) -> /ADC_DAC/DA6
- U5 pad 22: (no net) -> /ADC_DAC/DA7
- U5 pad 23: (no net) -> /ADC_DAC/DD0
- U5 pad 24: (no net) -> /ADC_DAC/DD1
- U5 pad 25: (no net) -> /ADC_DAC/DD2
- U5 pad 26: (no net) -> /ADC_DAC/DD3
- U5 pad 27: (no net) -> /ADC_DAC/DD4
- U5 pad 28: (no net) -> /ADC_DAC/DD5
- U5 pad 29: (no net) -> /ADC_DAC/DD6
- U5 pad 30: (no net) -> /ADC_DAC/DD7
- U5 pad 31: (no net) -> /ADC_DAC/DD8
- U5 pad 32: (no net) -> /ADC_DAC/DD9
- U5 pad 34: (no net) -> /ADC_DAC/SPI_MOSI
- U5 pad 35: (no net) -> /ADC_DAC/SPI_SCK
- U5 pad 36: (no net) -> /ADC_DAC/CS_AD
- U5 pad 38: (no net) -> Net-(U5-Pad38)
- U5 pad 47: /Anlg_Front_End/COM -> /ADC_DAC/COM
- U5 pad 48: /Anlg_Front_End/REFN -> /ADC_DAC/REFN
- U5 pad 7: (no net) -> Net-(U5-Pad7)
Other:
- board text removed: "A"
- board text removed: "K"

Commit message: 2xx40 conn
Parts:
- added J1: CONN_02X20, Pin_Headers:Pin_Header_Straight_2x20_Pitch2.54mm, F.Cu at (111.8, 52.5)
- moved GIO1 32.4 mm to (147.3, 75.3)
- moved S1 30.7 mm to (144.8, 102.0)
- moved U2 7.82 mm to (115.6, 141.4)
- moved L1 5.39 mm to (107.9, 135.0)
